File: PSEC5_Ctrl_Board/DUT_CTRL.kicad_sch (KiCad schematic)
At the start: 2 parts, among them J18 QSH-040-01-X-D-DP-A, J6 QSH-040-01-X-D-DP-A

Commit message: minor changes
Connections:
- net THRES6 is gone; now on net PICO: J6.11
- net THRES7 is gone; now on net READBIAS1: J6.13
- net THRES8 is gone; now on net READBIAS2: J6.15
- net ADC_SCLK: now also J18.24; no longer J18.29
- net ADC_SDO: now also J18.26; no longer J18.33
- net DAC_SCLK: now also J18.18; no longer J18.21
- net DAC_V_IN: now also J18.22; no longer J18.27
- net DISCBIAS: now also J6.19; no longer J6.39
- net OscRefClk: no longer J18.01
- net PICO: no longer J18.11
- net POCI: now also J6.04; no longer J18.09
- net Psec5RefClk: no longer J18.03
- net Psec5TriggerIn: now also J6.37; no longer J18.07
- net Psec5TriggerOut: now also J6.38; no longer J18.05
- net READBIAS1: no longer J6.33
- net READBIAS2: no longer J6.35
- net SIGNAL1+: now also J6.06; no longer J6.02
- net SIGNAL1-: now also J6.08; no longer J6.04
- net SIGNAL2+: now also J6.10; no longer J6.06
- net SIGNAL2-: now also J6.12; no longer J6.08
- net SIGNAL3+: now also J6.14; no longer J6.10
- net SIGNAL3-: now also J6.16; no longer J6.12
- net SIGNAL4+: now also J6.18; no longer J6.14
- net SIGNAL4-: now also J6.20; no longer J6.16
- net SIGNAL5+: now also J6.22; no longer J6.26
- net SIGNAL5-: now also J6.24; no longer J6.28
- net SIGNAL6+: now also J6.26; no longer J6.30
- net SIGNAL6-: now also J6.28; no longer J6.32
- net SIGNAL7+: now also J6.30; no longer J6.34
- net SIGNAL7-: now also J6.32; no longer J6.36
- net SIGNAL8+: now also J6.34; no longer J6.38
- net SIGNAL8-: now also J6.36; no longer J6.40
- net SYNC_N: now also J18.20; no longer J18.25
- net WBUFBIAS: now also J6.17; no longer J6.37
- net Disc_Thresh1: now reaches J6.21
- net Disc_Thresh2: now reaches J6.23
- net Disc_Thresh3: now reaches J6.25
- net Disc_Thresh4: now reaches J6.27
- net Disc_Thresh5: now reaches J6.29
- net Disc_Thresh6: now reaches J6.31
- net V_ped6: now reaches J18.12
- net V_ped7: now reaches J18.14
- net V_ped8: now reaches J18.16
- net ADC_CNV: now reaches J18.28
- net VDD12: now reaches J18.30
- net VDD18: now reaches J18.32
- net VDD33: now reaches J18.34
- net VDD25: now reaches J18.36
- net VDD50: now reaches J18.38
- net 1V2 renamed V_ped1
- net 1V8 renamed V_ped2
- net 2V5 renamed V_ped3
- net 3V3 renamed V_ped4
- net 5V renamed V_ped5
- net Psec5RST: no longer names the net of J18.15
- net Psec5ReadClk: no longer names the net of J18.17
- net SPIClk: no longer names the net of J18.13
- net THRES1: no longer names the net of J6.01
- net THRES2 renamed P5_ReadClk
- net THRES3: no longer names the net of J6.05
- net THRES4 renamed P5_rst
- net THRES5 renamed SPIclk
- new net Disc_Thresh7: J6.33
- new net Disc_Thresh8: J6.35
- no-connect marks 0 -> 23
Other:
- note added: "???????"
- moved on the sheet: J18A, J6A

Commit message: Schematic is "done" ;( (999+ ERC errors)
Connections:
- net Psec5RefClk: now also J6.40
- net OscClkOut: now reaches J18.40
- net VDD50: no longer names the net of J18.38
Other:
- note removed: "???????"

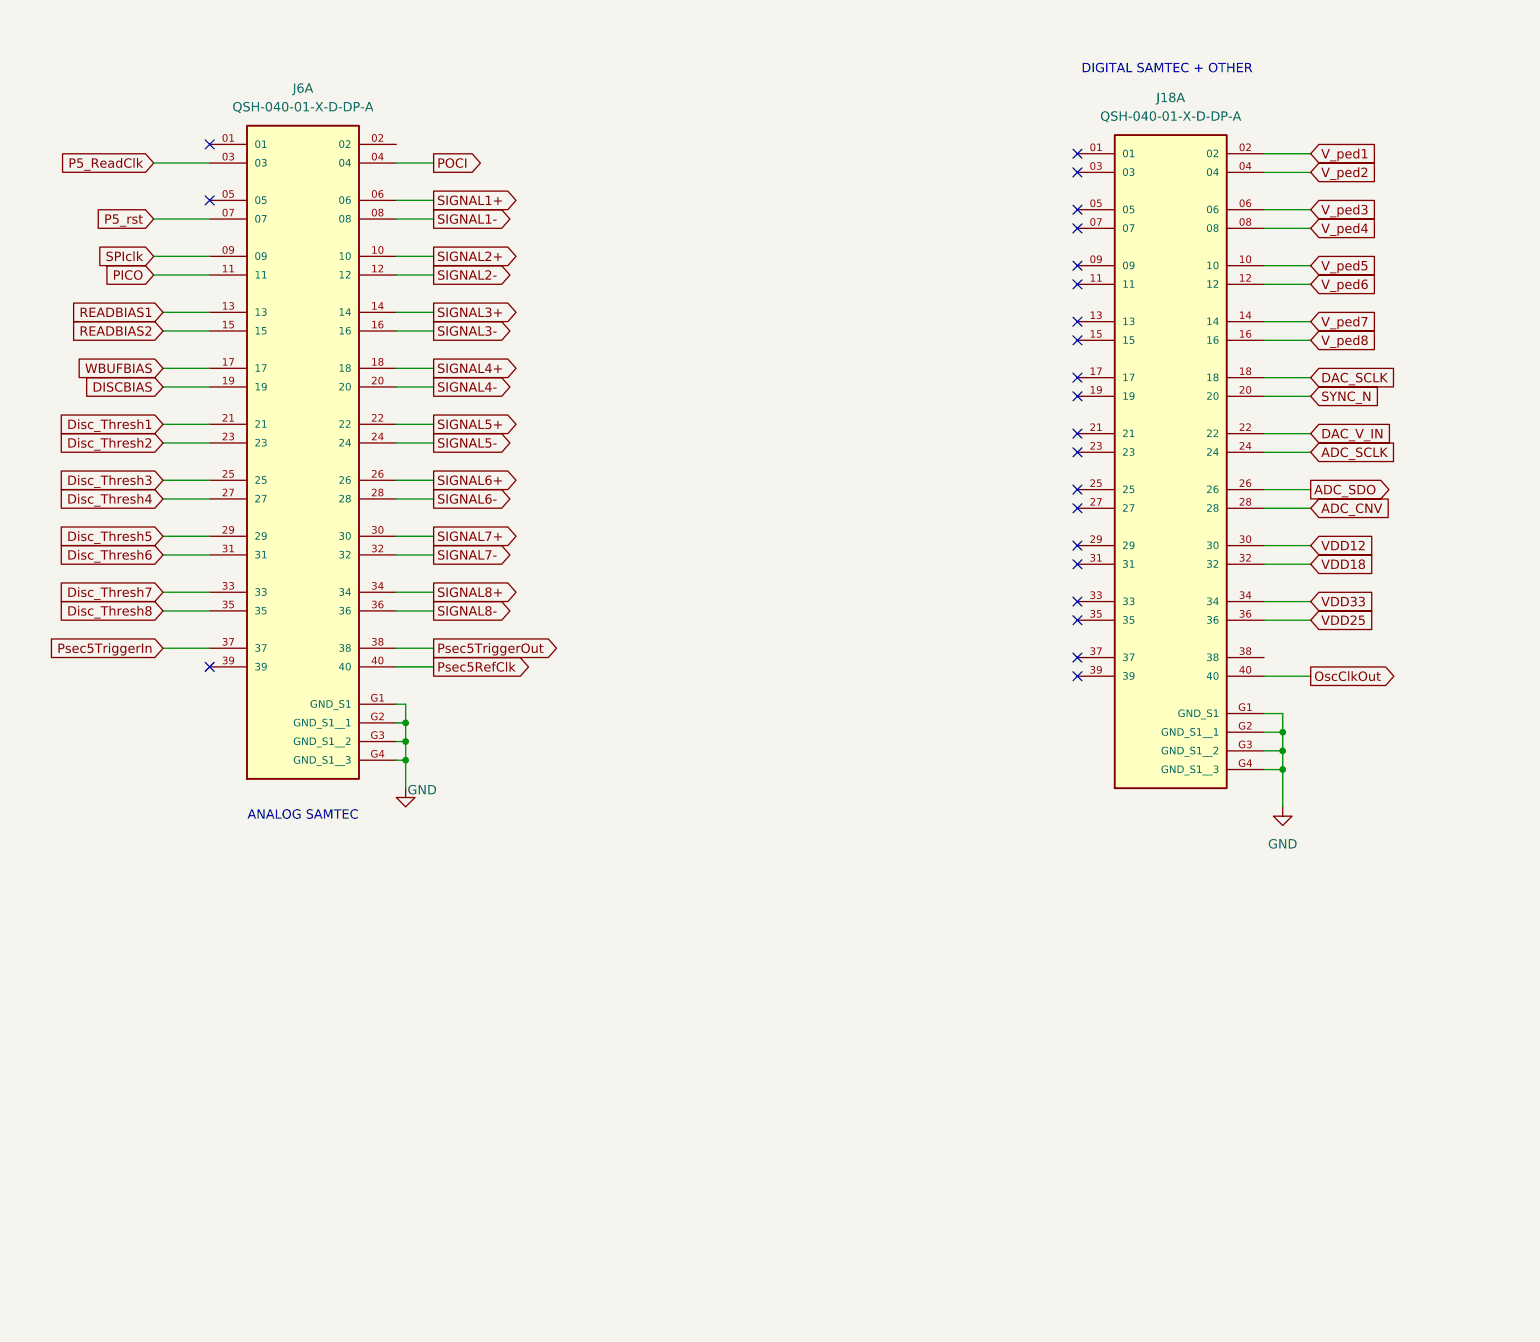
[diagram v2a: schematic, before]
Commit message: Deleted some Pages, still lots of errors :(
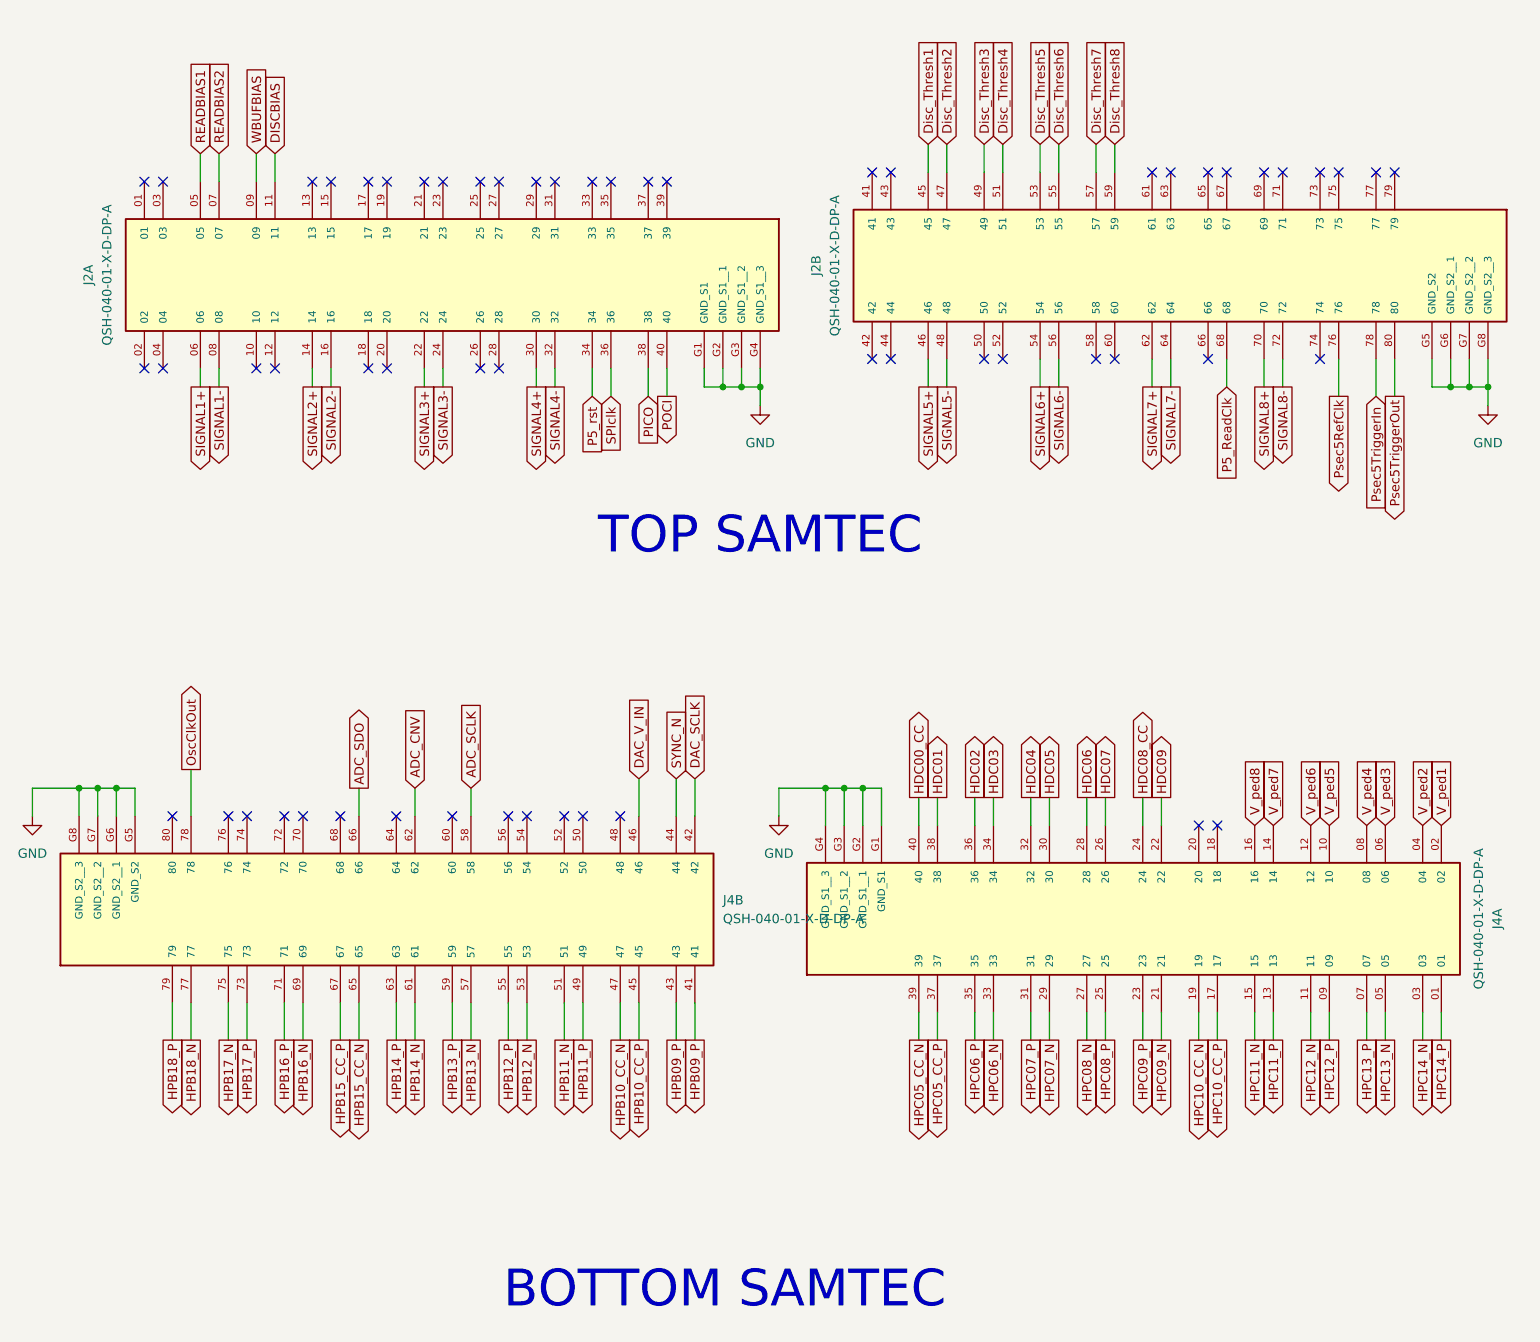
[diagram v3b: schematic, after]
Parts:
- removed J18, J6: QSH-040-01-X-D-DP-A, QSH-040-01-X-D-DP-A:SAMTEC_QSH-040-01-X-D-DP-A, symbol PSEC5_ctrlbd:QSH-040-01-X-D-DP-A
- added J2, J4: QSH-040-01-X-D-DP-A, QSH-040-01-X-D-DP-A:SAMTEC_QSH-040-01-X-D-DP-A, symbol PSEC5_ctrlbd:QSH-040-01-X-D-DP-A
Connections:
- net ADC_CNV: now also J4.62
- net ADC_SCLK: now also J4.58
- net ADC_SDO: now also J4.66
- net DAC_SCLK: now also J4.42
- net DAC_V_IN: now also J4.46
- net DISCBIAS: now also J2.11
- net Disc_Thresh1: now also J2.45
- net Disc_Thresh2: now also J2.47
- net Disc_Thresh3: now also J2.49
- net Disc_Thresh4: now also J2.51
- net Disc_Thresh5: now also J2.53
- net Disc_Thresh6: now also J2.55
- net Disc_Thresh7: now also J2.57
- net Disc_Thresh8: now also J2.59
- net GND: now also J2.G1 (GND_S1), J2.G2 (GND_S1__1), J2.G3 (GND_S1__2), J2.G4 (GND_S1__3), J2.G5 (GND_S2), J2.G6 (GND_S2__1), J2.G7 (GND_S2__2), J2.G8 (GND_S2__3), J4.G1 (GND_S1), J4.G2 (GND_S1__1), J4.G3 (GND_S1__2), J4.G4 (GND_S1__3), J4.G5 (GND_S2), J4.G6 (GND_S2__1), J4.G7 (GND_S2__2), J4.G8 (GND_S2__3)
- net OscClkOut: now also J4.78
- net P5_ReadClk: now also J2.68
- net P5_rst: now also J2.34
- net PICO: now also J2.38
- net POCI: now also J2.40
- net Psec5RefClk: now also J2.76
- net Psec5TriggerIn: now also J2.78
- net Psec5TriggerOut: now also J2.80
- net READBIAS1: now also J2.05
- net READBIAS2: now also J2.07
- net SIGNAL1+: now also J2.06
- net SIGNAL1-: now also J2.08
- net SIGNAL2+: now also J2.14
- net SIGNAL2-: now also J2.16
- net SIGNAL3+: now also J2.22
- net SIGNAL3-: now also J2.24
- net SIGNAL4+: now also J2.30
- net SIGNAL4-: now also J2.32
- net SIGNAL5+: now also J2.46
- net SIGNAL5-: now also J2.48
- net SIGNAL6+: now also J2.54
- net SIGNAL6-: now also J2.56
- net SIGNAL7+: now also J2.62
- net SIGNAL7-: now also J2.64
- net SIGNAL8+: now also J2.70
- net SIGNAL8-: now also J2.72
- net SPIclk: now also J2.36
- net SYNC_N: now also J4.44
- net V_ped1: now also J4.02
- net V_ped2: now also J4.04
- net V_ped3: now also J4.06
- net V_ped4: now also J4.08
- net V_ped5: now also J4.10
- net V_ped6: now also J4.12
- net V_ped7: now also J4.14
- net V_ped8: now also J4.16
- net WBUFBIAS: now also J2.09
- new net HDC00_CC: J4.40
- new net HDC01: J4.38
- new net HDC02: J4.36
- new net HDC03: J4.34
- new net HDC04: J4.32
- new net HDC05: J4.30
- new net HDC06: J4.28
- new net HDC07: J4.26
- new net HDC08_CC: J4.24
- new net HDC09: J4.22
- new net HPB09_P: J4.41, J4.43
- new net HPB10_CC_N: J4.47
- new net HPB10_CC_P: J4.45
- new net HPB11_N: J4.51
- new net HPB11_P: J4.49
- new net HPB12_N: J4.53
- new net HPB12_P: J4.55
- new net HPB13_N: J4.57
- new net HPB13_P: J4.59
- new net HPB14_N: J4.61
- new net HPB14_P: J4.63
- new net HPB15_CC_N: J4.65
- new net HPB15_CC_P: J4.67
- new net HPB16_N: J4.69
- new net HPB16_P: J4.71
- new net HPB17_N: J4.75
- new net HPB17_P: J4.73
- new net HPB18_N: J4.77
- new net HPB18_P: J4.79
- new net HPC05_CC_N: J4.39
- new net HPC05_CC_P: J4.37
- new net HPC06_N: J4.33
- new net HPC06_P: J4.35
- new net HPC07_N: J4.29
- new net HPC07_P: J4.31
- new net HPC08_N: J4.27
- new net HPC08_P: J4.25
- new net HPC09_N: J4.21
- new net HPC09_P: J4.23
- new net HPC10_CC_N: J4.19
- new net HPC10_CC_P: J4.17
- new net HPC11_N: J4.15
- new net HPC11_P: J4.13
- new net HPC12_N: J4.11
- new net HPC12_P: J4.09
- new net HPC13_N: J4.05
- new net HPC13_P: J4.07
- new net HPC14_N: J4.03
- new net HPC14_P: J4.01
- no-connect marks 23 -> 59
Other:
- note added: "BOTTOM SAMTEC"
- note added: "TOP SAMTEC"
- note removed: "ANALOG SAMTEC"
- note removed: "DIGITAL SAMTEC + OTHER"

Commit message: Minor Schematic Changes, ERC still haunts me :(
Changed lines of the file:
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@@
 	(text "BOTTOM SAMTEC\n"
 		(exclude_from_sim no)
-		(at 145.034 186.436 0)
+		(at 146.05 175.514 0)
 		(effects
 			(font
@@
 		(dnp no)
 		(property "Reference" "J4"
-			(at 144.78 133.3499 90)
+			(at 145.542 143.51 0)
 			(effects
 				(font
@@
 		)
 		(property "Value" "QSH-040-01-X-D-DP-A"
-			(at 144.78 135.8899 90)
-			(effects
-				(font
+			(at 148.082 143.51 0)
+			(effects
+				(font

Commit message: Changes
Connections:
- net ADC_CNV: now also J4.72; no longer J4.62
- net ADC_SCLK: now also J4.70; no longer J4.58
- net ADC_SDO: now also J4.76; no longer J4.66
- net DAC_Unused1: now reaches J2.17
- net DAC_Unused2: now reaches J2.19
- net DAC_Unused3: now reaches J2.21
- net DAC_Unused4: now reaches J2.23
- net 3V3_DUT: now reaches J4.54
- new net 1V2_DUT: J4.66
- new net 1V8_DUT: J4.62
- new net 2V5_DUT: J4.58
- no-connect marks 59 -> 51

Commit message: My PC is fading, pushing in case it dies
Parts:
- J2, J4: footprint QSH-040-01-X-D-DP-A:SAMTEC_QSH-040-01-X-D-DP-A -> QSH-040-01-L-D-DP-A:SAMTEC_QSH-040-01-X-D-DP-A
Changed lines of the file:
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@@
 			)
 		)
-		(property "Footprint" "QSH-040-01-X-D-DP-A:SAMTEC_QSH-040-01-X-D-DP-A"
+		(property "Footprint" "QSH-040-01-L-D-DP-A:SAMTEC_QSH-040-01-X-D-DP-A"
 			(at 59.69 54.102 0)
 			(effects
@@
 			)
 		)
-		(property "Footprint" "QSH-040-01-X-D-DP-A:SAMTEC_QSH-040-01-X-D-DP-A"
+		(property "Footprint" "QSH-040-01-L-D-DP-A:SAMTEC_QSH-040-01-X-D-DP-A"
 			(at 158.75 52.832 0)
 			(effects
@@
 			)
 		)
-		(property "Footprint" "QSH-040-01-X-D-DP-A:SAMTEC_QSH-040-01-X-D-DP-A"
+		(property "Footprint" "QSH-040-01-L-D-DP-A:SAMTEC_QSH-040-01-X-D-DP-A"
 			(at 147.32 128.778 0)
 			(effects
@@
 			)
 		)
-		(property "Footprint" "QSH-040-01-X-D-DP-A:SAMTEC_QSH-040-01-X-D-DP-A"
+		(property "Footprint" "QSH-040-01-L-D-DP-A:SAMTEC_QSH-040-01-X-D-DP-A"
 			(at 248.92 130.048 0)
 			(effects
